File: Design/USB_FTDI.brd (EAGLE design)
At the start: 32.7 x 14.6 mm, 24 parts, among them IC1 FT232RL-REEL, J1 USB1061-GF-L-A, U1 LM3940IMP-3.3

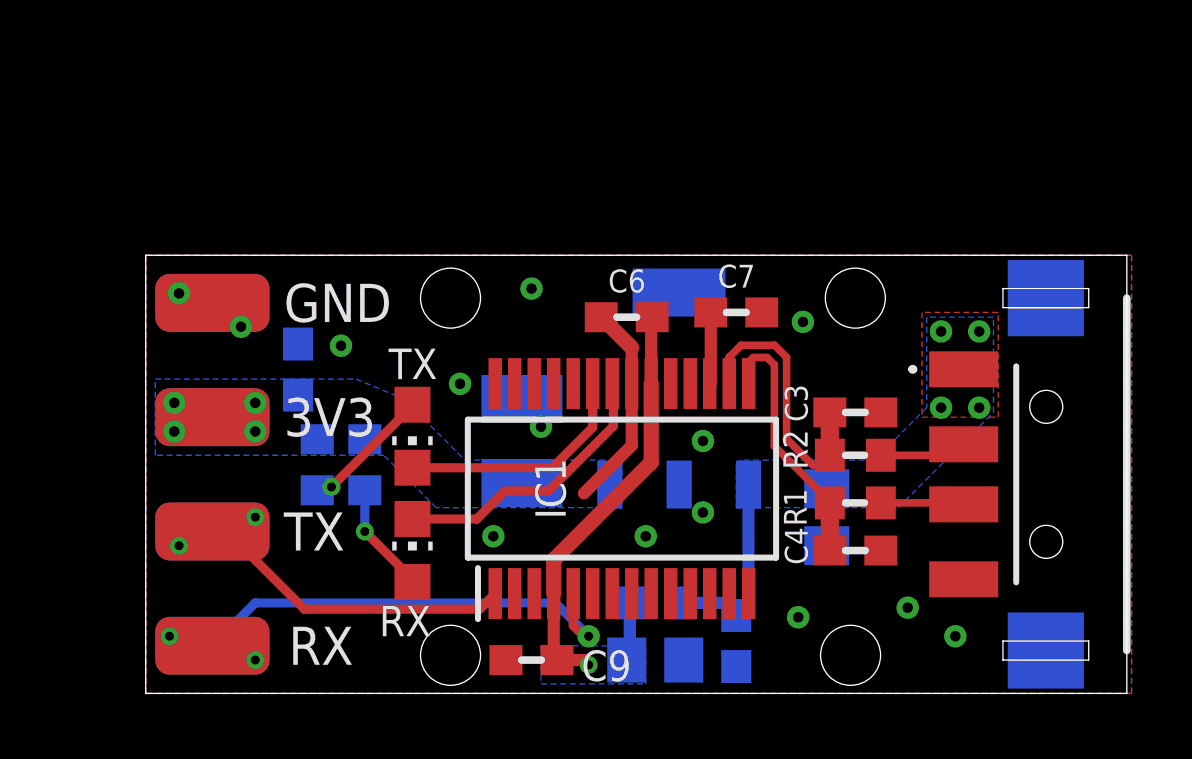
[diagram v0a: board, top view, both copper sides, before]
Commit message: - Connect the VCCIO pin of the FTDI IC to the 3.3V - Improve the layout to offer better thermal conductivity for the LDO
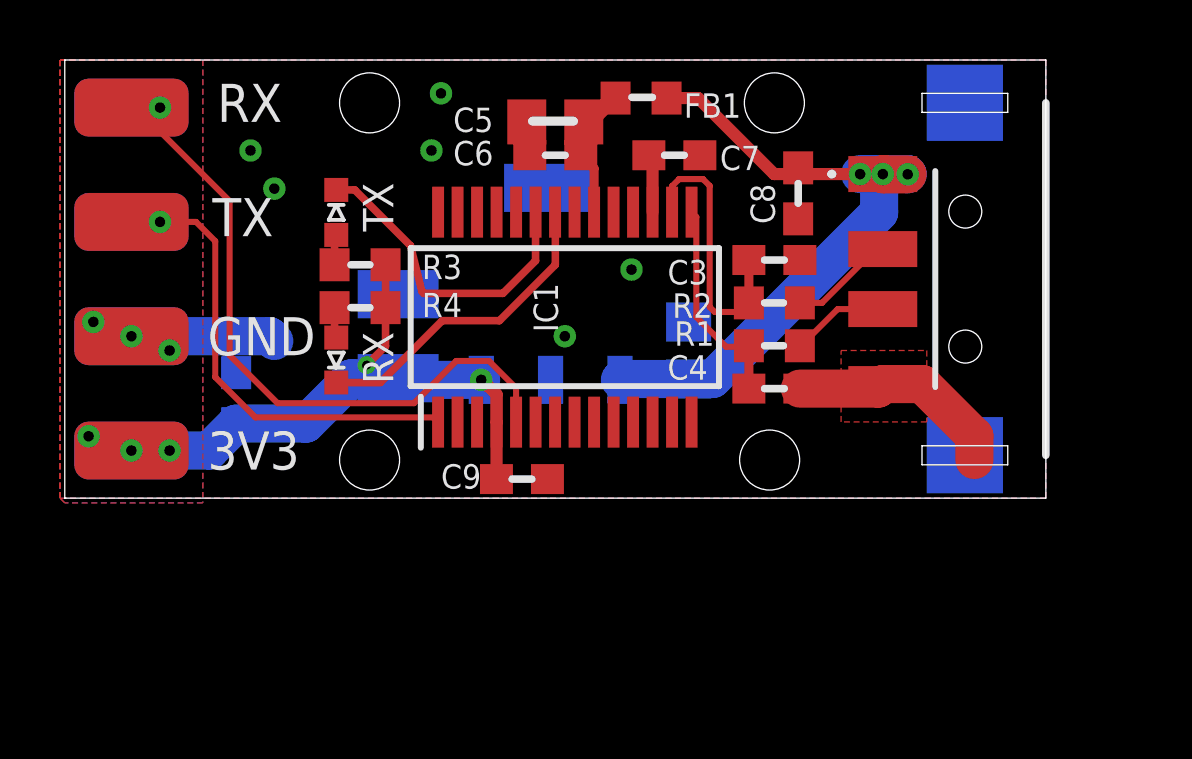
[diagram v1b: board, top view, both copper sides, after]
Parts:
- added TRIMBLE-LOGO1: HEXA-LOGO, HEXABITZ_USER_INTERFACE_PARTS:HEXA-LOGO
- C5: device HEXABITZ_RCLS:C-0805-POL -> HEXABITZ_RCLS:C-0805
- RXLED: value Orange -> RED; device HEXABITZ_USER_INTERFACE_PARTS:CHIP-LED0805 -> HEXABITZ_USER_INTERFACE_PARTS:VLMS1300-GS08
- TXLED: value Yellow -> RED; device HEXABITZ_USER_INTERFACE_PARTS:CHIP-LED0805 -> HEXABITZ_USER_INTERFACE_PARTS:VLMS1300-GS08
- moved C5 18.2 mm to (0.16, 12.5), flipped to the top
- moved RX 18.1 mm to (-14.0, 13.0)
- moved FB1 16.8 mm to (3.02, 13.3), flipped to the top, turned to 180 degrees
- moved C8 15.1 mm to (8.26, 10.2), flipped to the top
- moved TX 10.7 mm to (-14.0, 9.21)
- moved TXLED 7.88 mm to (-7.14, 9.53)
- moved C2 7.22 mm to (4.60, 4.92), turned to 90 degrees
- moved J1 7.05 mm to (22.2, 7.30)
- moved RXLED 6.84 mm to (-7.14, 4.60)
- moved R3 6.82 mm to (-6.35, 7.78), flipped to the top, turned to 0 degrees
- moved C9 6.04 mm to (-0.95, 0.64), turned to 0 degrees
- moved C4 6.03 mm to (7.46, 3.65)
- moved IC1 6.02 mm to (0.48, 6.03)
- moved C6 5.90 mm to (0.16, 11.4)
- moved R1 5.89 mm to (7.46, 5.08)
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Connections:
- net +3V3: now also C9.1, IC1.4
- net N$5: no longer C9.1, IC1.4
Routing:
- net +3V3: track 3.25 -> 25.6 mm, vias 4 -> 5
- net +5V: track 6.55 -> 24.2 mm, vias 4 -> 3
- net N$5: track 15.9 -> 4.94 mm, vias 1 -> 0
- net GND: track 6.96 -> 15.2 mm, vias 14 -> 9
- net N$4: track 20.1 -> 23.9 mm, vias 3 -> 1
- net N$2: track 4.38 -> 1.02 mm, vias 1 -> 0
- net N$1: track 3.72 -> 1.02 mm, vias 1 -> 0
- net N$6: track 8.03 -> 10.7 mm
- net USBF_P: track 8.70 -> 7.15 mm
- net N$3: track 15.3 -> 16.6 mm, vias 2 -> 1
- net N$7: track 9.41 -> 10.7 mm
- net USB_N: track 2.91 -> 3.51 mm
- removed copper zone on layer 16, net +3V3
- removed copper zone on layer 1, net +5V
- removed copper zone on layer 16, net +5V
- removed copper zone on layer 16, net N$5
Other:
- board text added: "FTDI_V1"
- board text removed: "FTDI_V0"
